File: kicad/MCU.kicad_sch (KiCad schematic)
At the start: 9 parts, among them U10 STM32G0B1R_B-C-E_Tx, U34 SN65HVD230, Y2 CM9V-T1A 32.768 kHz

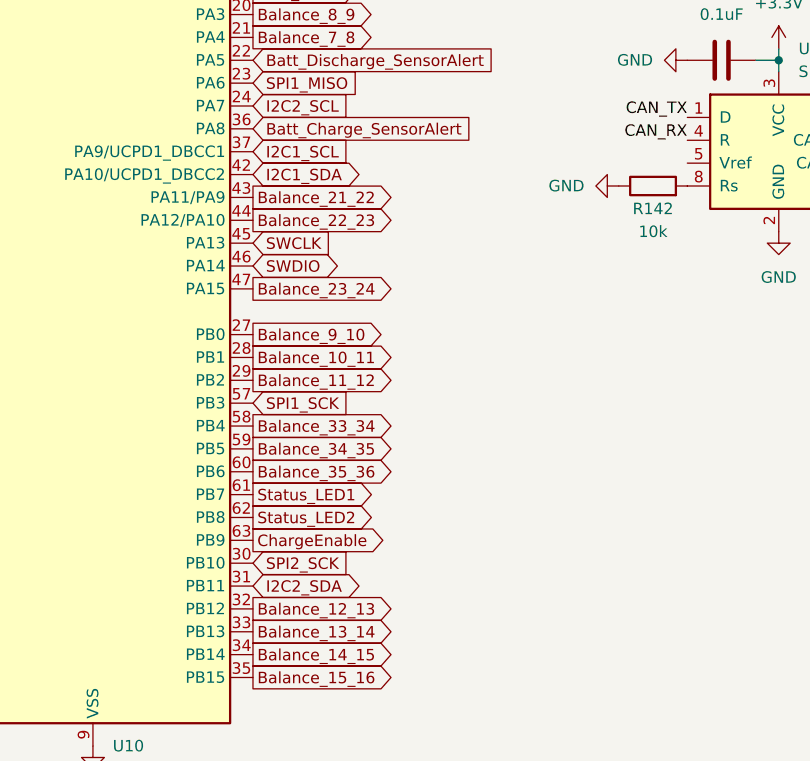
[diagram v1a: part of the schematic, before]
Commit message: implemented cell balancing up to 16S
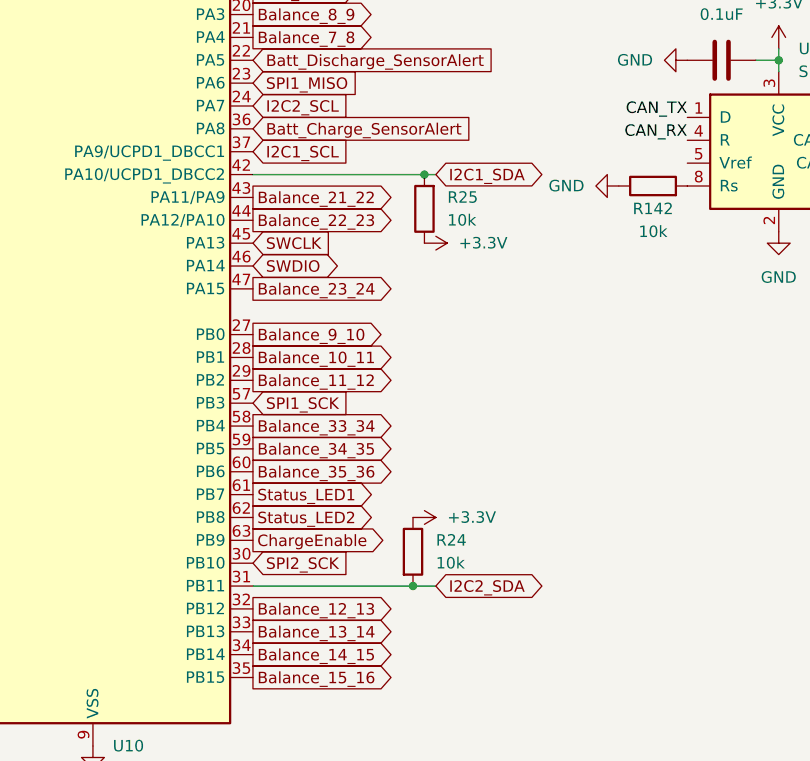
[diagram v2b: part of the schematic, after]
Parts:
- added R24, R25: 10k, symbol Device:R
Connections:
- net +3.3V: now also R24.1, R25.1
- net I2C1_SDA: now also R25.2
- net I2C2_SDA: now also R24.2
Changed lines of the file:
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@@
     (comment 1 "All about the STM32")
   )
+  (junction (at 90.17 59.69) (diameter 0) (color 0 0 0 0)
+  )
   (junction (at 53.34 24.13) (diameter 0) (color 0 0 0 0)
   )
+  (junction (at 88.9 105.41) (diameter 0) (color 0 0 0 0)
+  )
   (junction (at 129.54 46.99) (diameter 0) (color 0 0 0 0)
   )
@@
     (stroke (width 0) (type default))
   )
+  (wire (pts (xy 91.44 59.69) (xy 90.17 59.69))
+    (stroke (width 0) (type default))
+  )
   (wire (pts (xy 29.21 34.29) (xy 31.75 34.29))
     (stroke (width 0) (type default))
   )
+  (wire (pts (xy 90.17 59.69) (xy 71.12 59.69))
+    (stroke (width 0) (type default))
+  )
   (wire (pts (xy 171.45 59.69) (xy 171.45 57.15))
     (stroke (width 0) (type default))
   )
+  (wire (pts (xy 71.12 105.41) (xy 88.9 105.41))
+    (stroke (width 0) (type default))
+  )
   (wire (pts (xy 181.61 59.69) (xy 181.61 57.15))
     (stroke (width 0) (type default))
@@
   )
   (wire (pts (xy 129.54 45.72) (xy 129.54 46.99))
+    (stroke (width 0) (type default))
+  )
+  (wire (pts (xy 91.44 105.41) (xy 88.9 105.41))
     (stroke (width 0) (type default))
   )
@@
     )
   )
-  (global_label "I2C2_SDA" (shape bidirectional) (at 71.12 105.41 0) (fields_autoplaced)
-    (effects (font (size 1.27 1.27)) (justify left))
-    (property "Intersheetrefs" "${INTERSHEET_REFS}" (at 84.046 105.41 0)
+  (global_label "I2C2_SDA" (shape bidirectional) (at 91.44 105.41 0) (fields_autoplaced)
+    (effects (font (size 1.27 1.27)) (justify left))
+    (property "Intersheetrefs" "${INTERSHEET_REFS}" (at 104.366 105.41 0)
       (effects (font (size 1.27 1.27)) (justify left) hide)
     )
@@
     )
   )
-  (global_label "I2C1_SDA" (shape bidirectional) (at 71.12 59.69 0) (fields_autoplaced)
-    (effects (font (size 1.27 1.27)) (justify left))
-    (property "Intersheetrefs" "${INTERSHEET_REFS}" (at 84.046 59.69 0)
+  (global_label "I2C1_SDA" (shape bidirectional) (at 91.44 59.69 0) (fields_autoplaced)
+    (effects (font (size 1.27 1.27)) (justify left))
+    (property "Intersheetrefs" "${INTERSHEET_REFS}" (at 104.366 59.69 0)
       (effects (font (size 1.27 1.27)) (justify left) hide)
     )
@@
     (property "Intersheetrefs" "${INTERSHEET_REFS}" (at 23.201 87.63 0)
       (effects (font (size 1.27 1.27)) (justify right) hide)
+    )
+  )
+  (symbol (lib_id "Device:R") (at 88.9 101.6 0) (unit 1)
+    (in_bom yes) (on_board yes) (dnp no) (fields_autoplaced)
+    (property "Reference" "R24" (at 91.44 100.33 0)
+      (effects (font (size 1.27 1.27)) (justify left))
+    )
+    (property "Value" "10k" (at 91.44 102.87 0)
+      (effects (font (size 1.27 1.27)) (justify left))
+    )
+    (property "Footprint" "" (at 87.122 101.6 90)
+      (effects (font (size 1.27 1.27)) hide)
+    )
+    (property "Datasheet" "~" (at 88.9 101.6 0)
+      (effects (font (size 1.27 1.27)) hide)
+    )
+    (pin "1")
+    (pin "2")
+    (instances
+      (project "sBMS"
+        (path "/7f25f26f-13d1-483f-a85d-b3abae309e30/bb4c6abb-96c2-4de6-af9e-637895d0c9f4"
+          (reference "R24") (unit 1)
+        )
+      )
     )
   )
@@
         (path "/7f25f26f-13d1-483f-a85d-b3abae309e30/bb4c6abb-96c2-4de6-af9e-637895d0c9f4"
           (reference "#PWR06") (unit 1)
+        )
+      )
+    )
+  )
+  (symbol (lib_id "power:+3.3V") (at 90.17 67.31 270) (unit 1)
+    (in_bom yes) (on_board yes) (dnp no) (fields_autoplaced)
+    (property "Reference" "#PWR081" (at 86.36 67.31 0)
+      (effects (font (size 1.27 1.27)) hide)
+    )
+    (property "Value" "+3.3V" (at 93.98 67.31 90)
+      (effects (font (size 1.27 1.27)) (justify left))
+    )
+    (property "Footprint" "" (at 90.17 67.31 0)
+      (effects (font (size 1.27 1.27)) hide)
+    )
+    (property "Datasheet" "" (at 90.17 67.31 0)
+      (effects (font (size 1.27 1.27)) hide)
+    )
+    (pin "1")
+    (instances
+      (project "sBMS"
+        (path "/7f25f26f-13d1-483f-a85d-b3abae309e30/bb4c6abb-96c2-4de6-af9e-637895d0c9f4"
+          (reference "#PWR081") (unit 1)
         )
       )
@@
     )
   )
+  (symbol (lib_id "Device:R") (at 90.17 63.5 180) (unit 1)
+    (in_bom yes) (on_board yes) (dnp no) (fields_autoplaced)
+    (property "Reference" "R25" (at 92.71 62.23 0)
+      (effects (font (size 1.27 1.27)) (justify right))
+    )
+    (property "Value" "10k" (at 92.71 64.77 0)
+      (effects (font (size 1.27 1.27)) (justify right))
+    )
+    (property "Footprint" "" (at 91.948 63.5 90)
+      (effects (font (size 1.27 1.27)) hide)
+    )
+    (property "Datasheet" "~" (at 90.17 63.5 0)
+      (effects (font (size 1.27 1.27)) hide)
+    )
+    (pin "1")
+    (pin "2")
+    (instances
+      (project "sBMS"
+        (path "/7f25f26f-13d1-483f-a85d-b3abae309e30/bb4c6abb-96c2-4de6-af9e-637895d0c9f4"
+          (reference "R25") (unit 1)
+        )
+      )
+    )
+  )
   (symbol (lib_id "power:+3.3V") (at 129.54 45.72 0) (unit 1)
     (in_bom yes) (on_board yes) (dnp no) (fields_autoplaced)
@@
         )
       )
+    )
+  )
+  (symbol (lib_id "power:+3.3V") (at 88.9 97.79 270) (unit 1)
+    (in_bom yes) (on_board yes) (dnp no) (fields_autoplaced)
+    (property "Reference" "#PWR080" (at 85.09 97.79 0)
+      (effects (font (size 1.27 1.27)) hide)
+    )
+    (property "Value" "+3.3V" (at 92.71 97.79 90)
+      (effects (font (size 1.27 1.27)) (justify left))
+    )
+    (property "Footprint" "" (at 88.9 97.79 0)
+      (effects (font (size 1.27 1.27)) hide)
+    )
+    (property "Datasheet" "" (at 88.9 97.79 0)
+      (effects (font (size 1.27 1.27)) hide)
+    )
+    (pin "1")
+    (instances
+      (project "sBMS"
+        (path "/7f25f26f-13d1-483f-a85d-b3abae309e30/bb4c6abb-96c2-4de6-af9e-637895d0c9f4"
+          (reference "#PWR080") (unit 1)
+        )
+      )

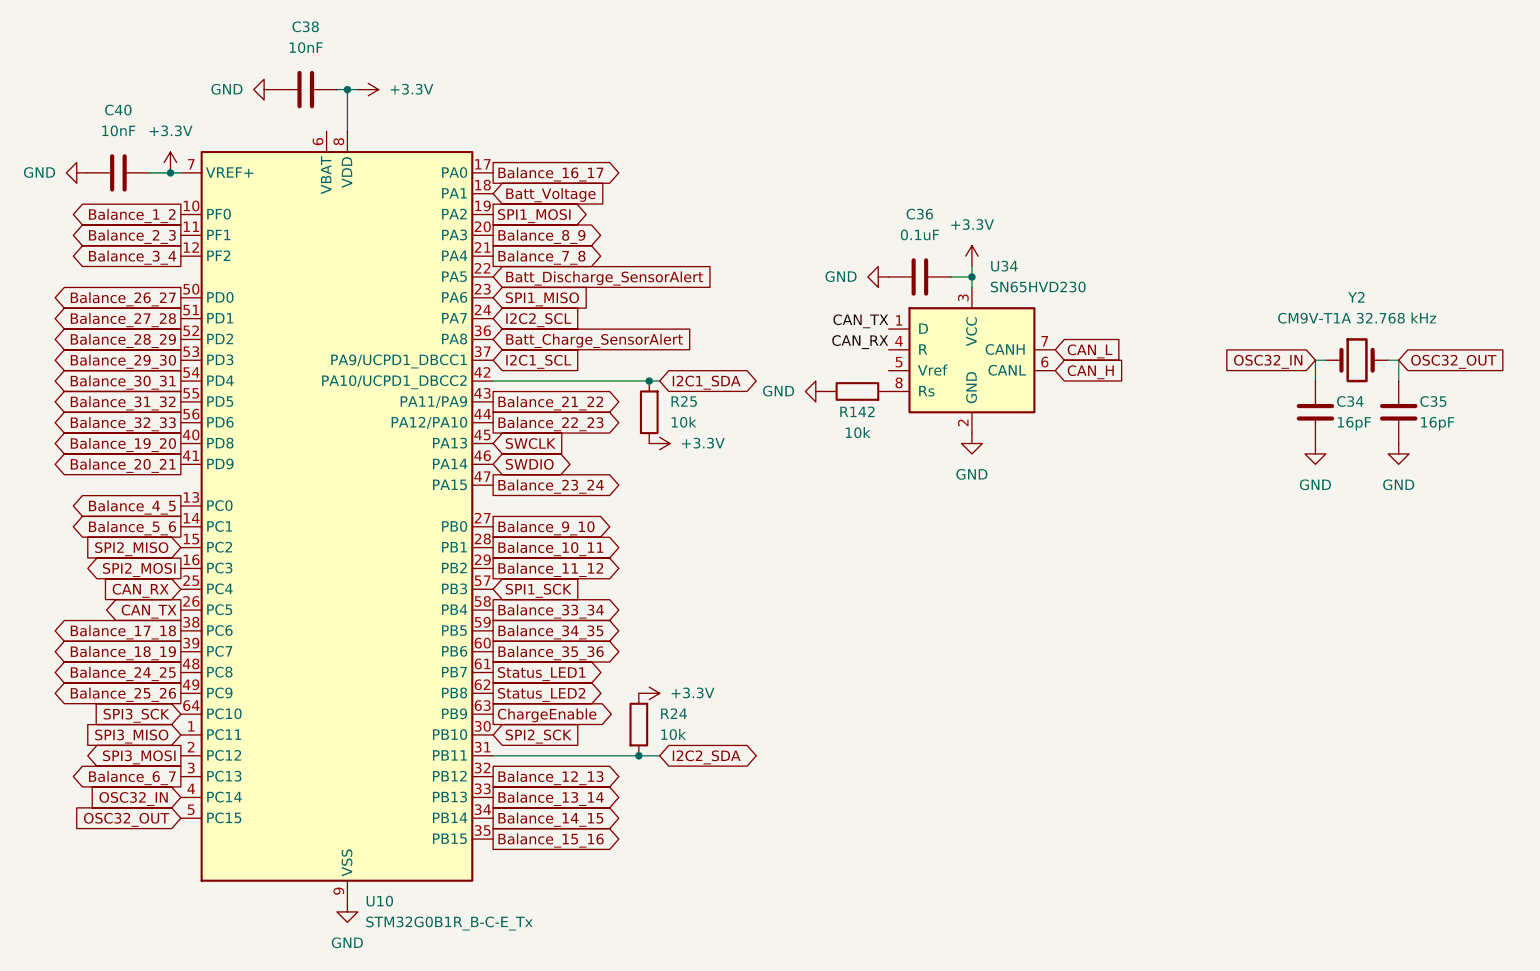
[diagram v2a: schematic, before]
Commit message: made full cell balancing up to 36S
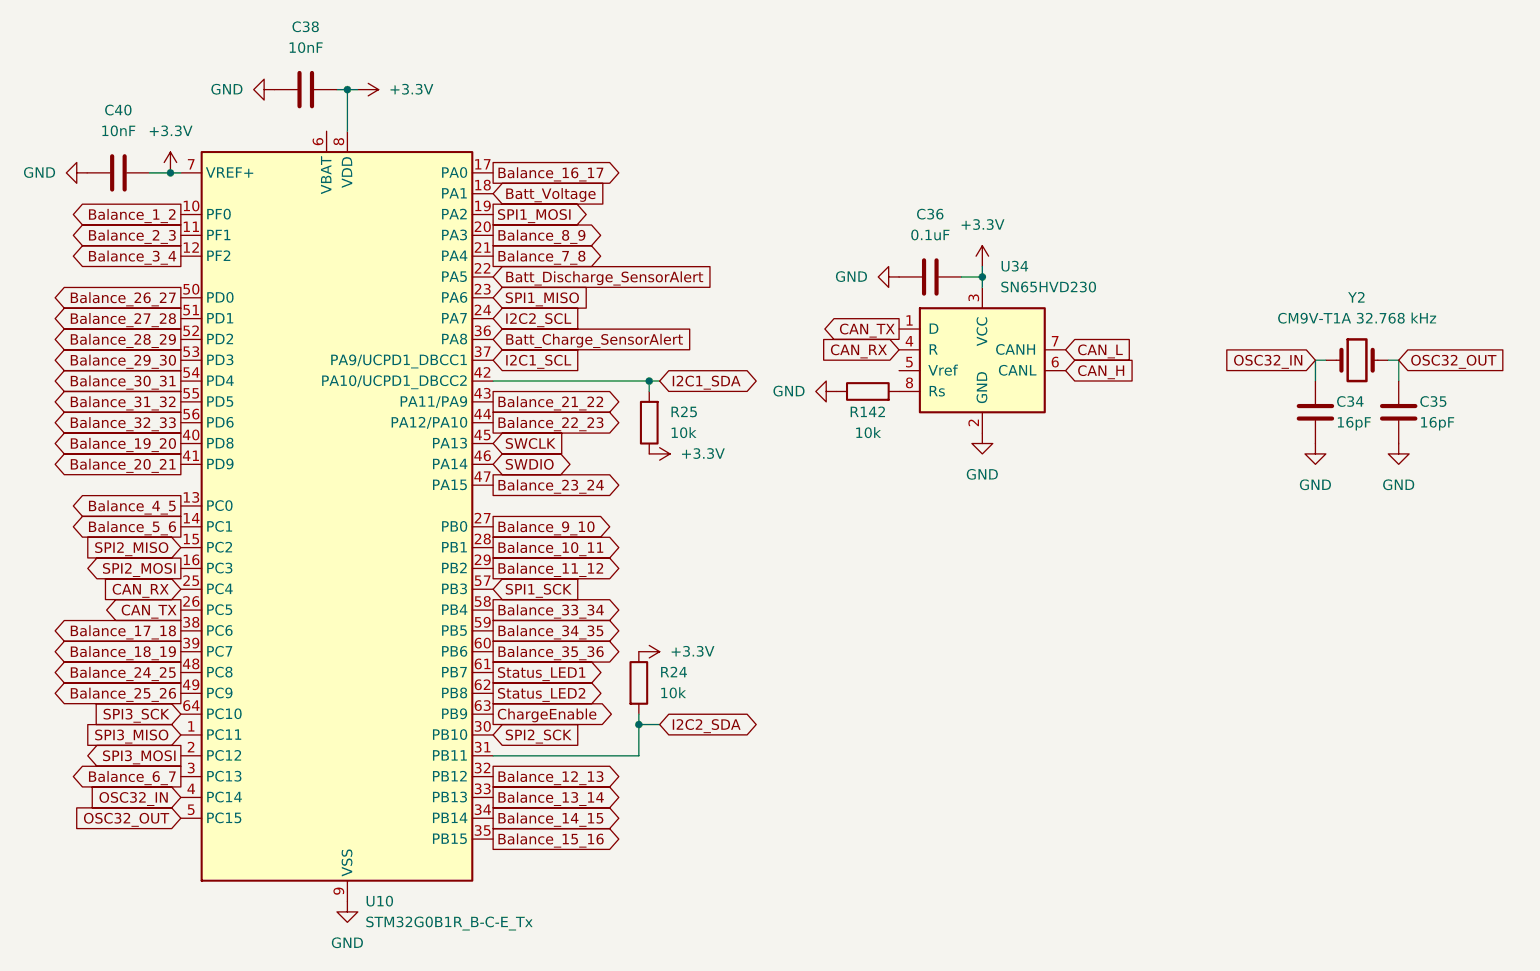
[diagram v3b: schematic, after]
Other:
- moved on the sheet: C36, R142, R24, R25, U34

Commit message: Replaced STM32G0B1RBTx with STM32G0B1KCUx, simplified balancing control
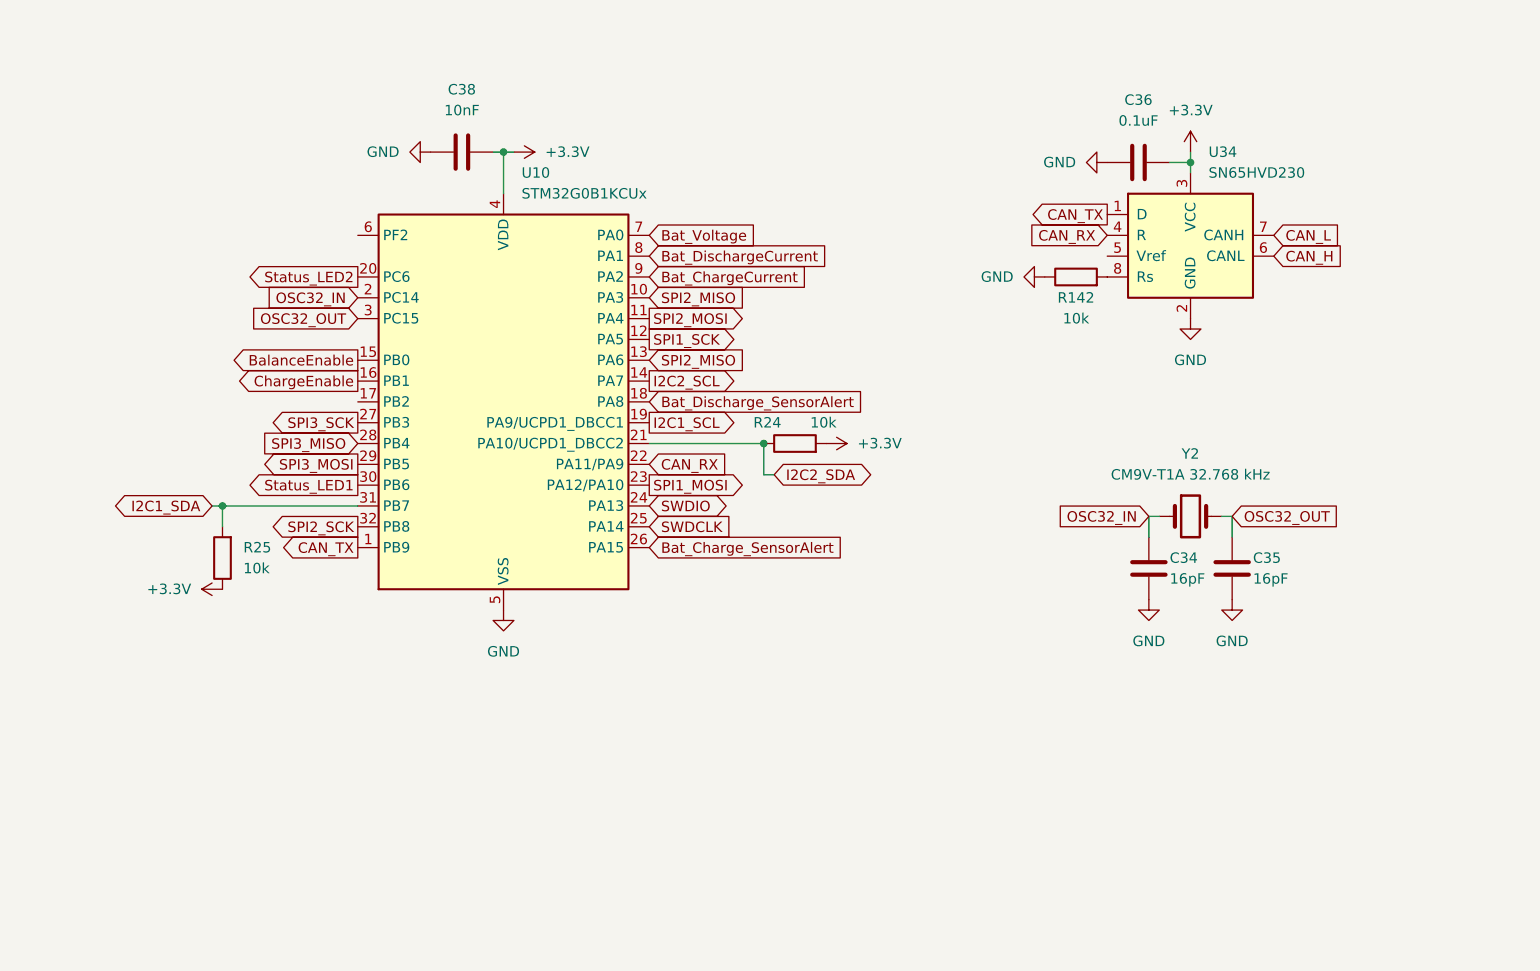
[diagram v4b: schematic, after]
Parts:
- removed C40: 10nF, symbol Device:C
- removed U10: STM32G0B1R_B-C-E_Tx, Package_QFP:LQFP-64_10x10mm_P0.5mm, symbol MCU_ST_STM32G0:STM32G0B1R_B-C-E_Tx
- added U10: STM32G0B1KCUx, Package_DFN_QFN:QFN-32-1EP_5x5mm_P0.5mm_EP3.45x3.45mm, symbol MCU_ST_STM32G0:STM32G0B1KCUx
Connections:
- net +3.3V: now also R24.2, U10.4 (VDD); no longer R24.1
- net CAN_RX: now also U10.22 (PA11/PA9)
- net CAN_TX: now also U10.1 (PB9)
- net ChargeEnable: now also U10.16 (PB1)
- net GND: now also U10.33 (VSS), U10.5 (VSS)
- net I2C1_SCL: now also U10.19 (PA9/UCPD1_DBCC1)
- net I2C1_SDA: now also U10.31 (PB7)
- net I2C2_SCL: now also U10.14 (PA7)
- net I2C2_SDA: now also R24.1, U10.21 (PA10/UCPD1_DBCC2); no longer R24.2
- net OSC32_IN: now also U10.2 (PC14)
- net OSC32_OUT: now also U10.3 (PC15)
- net SPI1_MOSI: now also U10.23 (PA12/PA10)
- net SPI1_SCK: now also U10.12 (PA5)
- net SPI2_MISO: now also U10.10 (PA3), U10.13 (PA6)
- net SPI2_MOSI: now also U10.11 (PA4)
- net SPI2_SCK: now also U10.32 (PB8)
- net SPI3_MISO: now also U10.28 (PB4)
- net SPI3_MOSI: now also U10.29 (PB5)
- net SPI3_SCK: now also U10.27 (PB3)
- net SWDIO: now also U10.24 (PA13)
- net Status_LED1: now also U10.30 (PB6)
- net Status_LED2: now also U10.20 (PC6)
- new net BalanceEnable: U10.15 (PB0)
- new net Bat_ChargeCurrent: U10.9 (PA2)
- new net Bat_Charge_SensorAlert: U10.26 (PA15)
- new net Bat_DischargeCurrent: U10.8 (PA1)
- new net Bat_Discharge_SensorAlert: U10.18 (PA8)
- new net Bat_Voltage: U10.7 (PA0)
- new net SWDCLK: U10.25 (PA14)
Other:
- moved on the sheet: C34, C35, C36, R142, U34, Y2
